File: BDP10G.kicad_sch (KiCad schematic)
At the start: 51 parts, among them J10 FPC40_0.5_DIRECT BDP10G, J12 Hirose_FH12-40S-0.5SH_1x40-1M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, Q12 D882, Q13 D882, U1 AMS1117-5.0, U12 L293WS(XBLW), U16 LM324DT

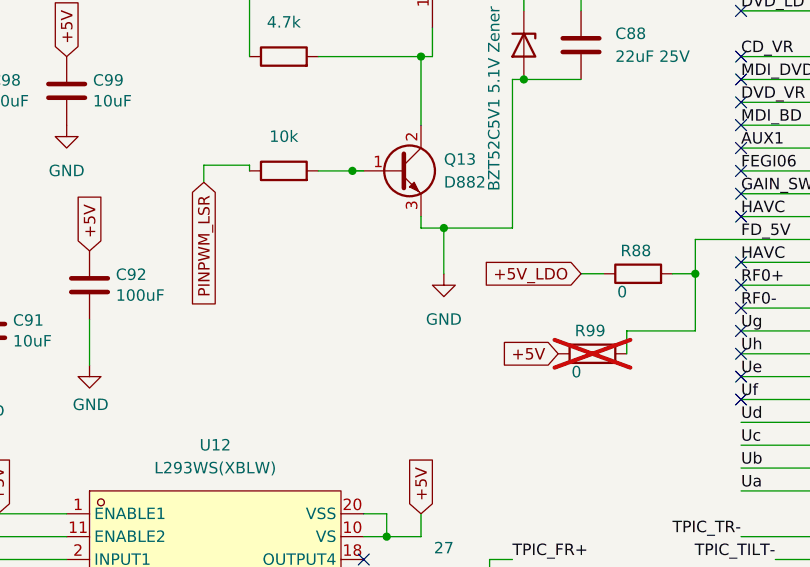
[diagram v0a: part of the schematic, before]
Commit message: fix work for piezo and step driver
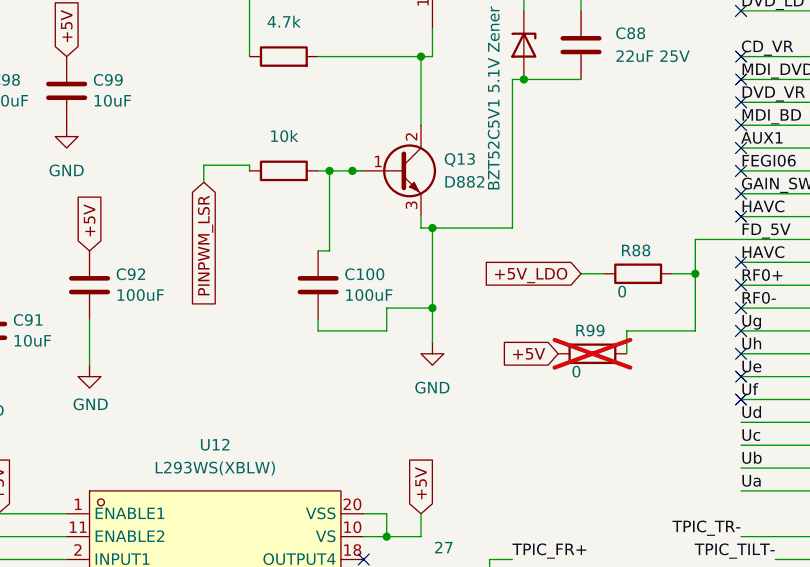
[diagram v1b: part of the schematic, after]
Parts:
- added C100: 100uF, piezo_driver:C_1206_3216Metric_u, symbol piezo_driver:C
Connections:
- net GND: now also C100.2
- net at Q13.1 (B), R17.2: now also C100.1
